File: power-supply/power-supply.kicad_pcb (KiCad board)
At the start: 2 copper layers, 100 x 100 mm, 22 parts, among them J1 Screw_Terminal_01x02, J2 Conn_01x03, J3 Conn_01x03, J4 Conn_01x03, J5 Conn_01x03, J6 Conn_01x03, J7 Conn_01x03, U1 L7815, U2 L7915

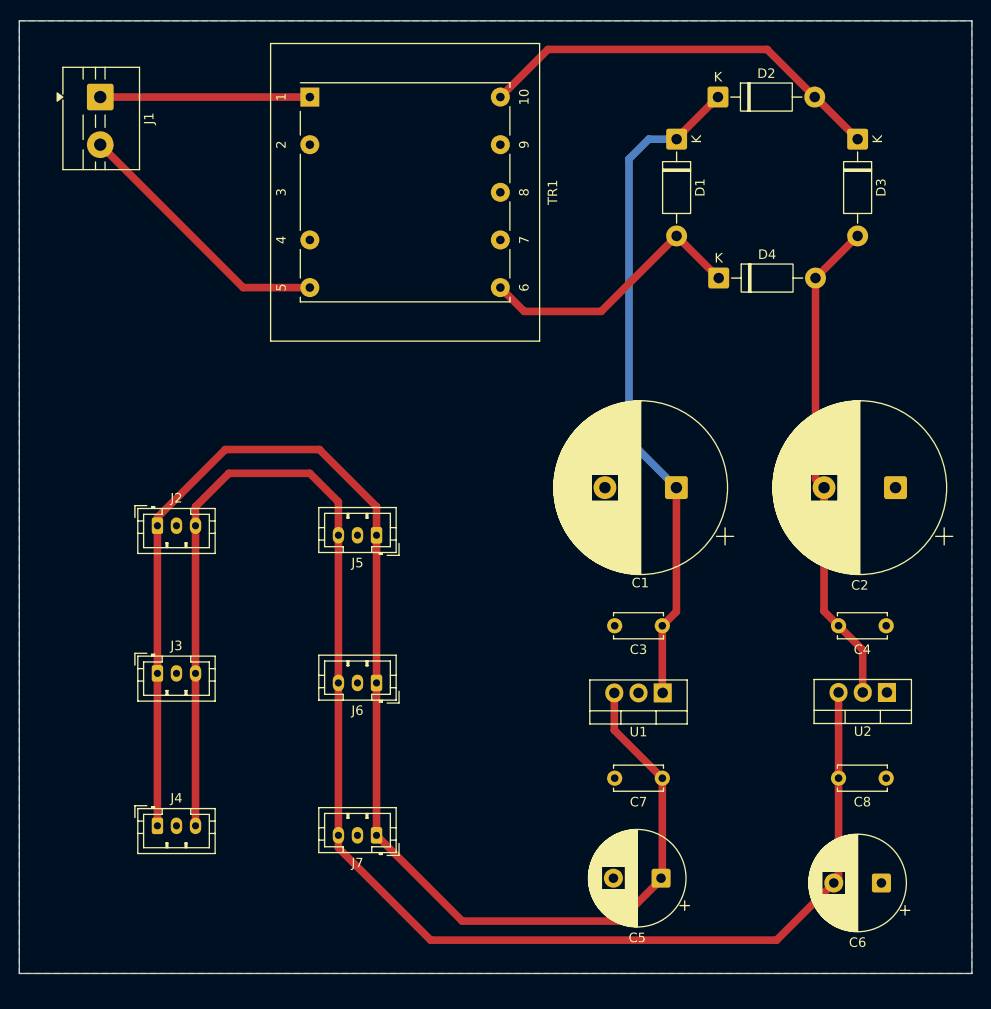
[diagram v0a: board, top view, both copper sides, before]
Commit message: power-supply: Improved version
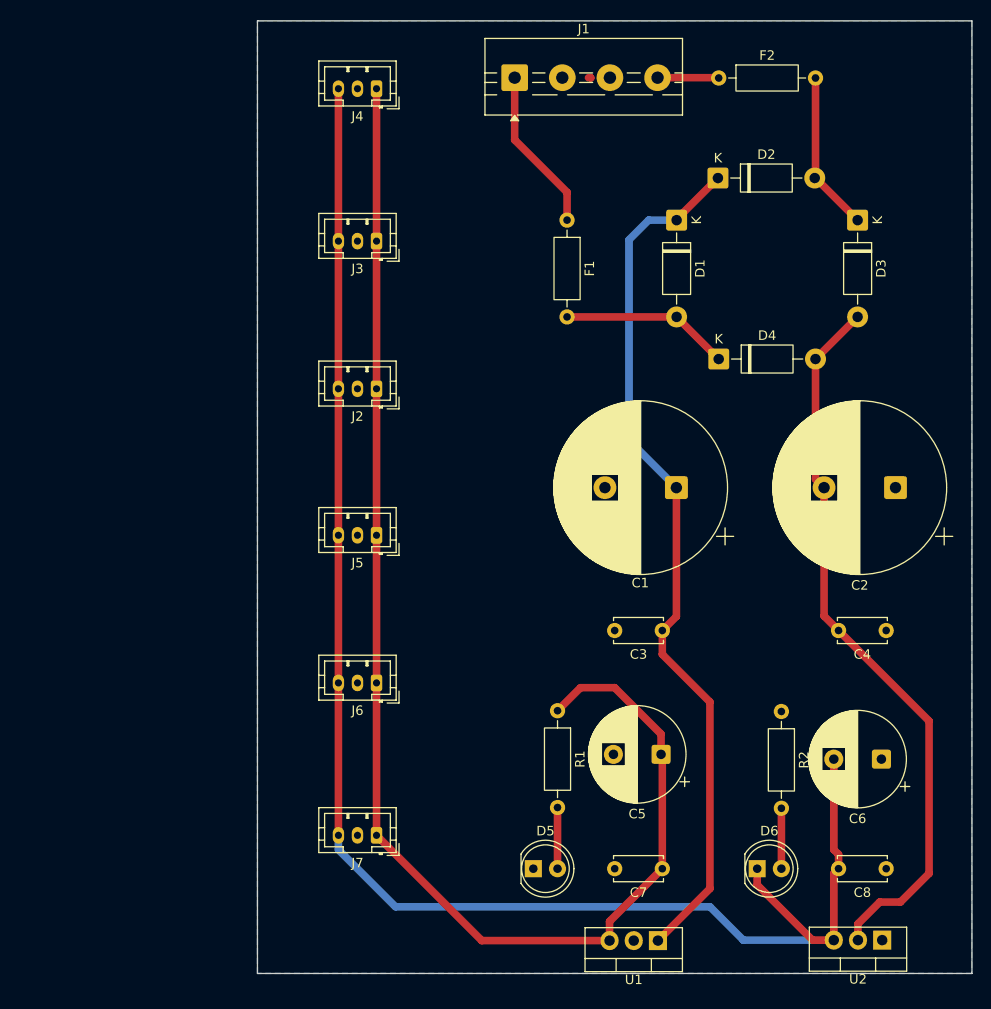
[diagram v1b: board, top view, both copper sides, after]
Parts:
- removed TR1: TEZ2.5/D230/18-18V, Transformer_THT:Transformer_Breve_TEZ-28x33
- added D5: LED, LED_THT:LED_D5.0mm, F.Cu at (204.0, 139.0)
- added D6: LED, LED_THT:LED_D5.0mm, F.Cu at (227.5, 139.0)
- added F1: Fuse, Resistor_THT:R_Axial_DIN0207_L6.3mm_D2.5mm_P10.16mm_Horizontal, F.Cu at (207.5, 70.9)
- added F2: Fuse, Resistor_THT:R_Axial_DIN0207_L6.3mm_D2.5mm_P10.16mm_Horizontal, F.Cu at (223.4, 56.0)
- added R1: R, Resistor_THT:R_Axial_DIN0207_L6.3mm_D2.5mm_P10.16mm_Horizontal, F.Cu at (206.5, 122.4)
- added R2: R, Resistor_THT:R_Axial_DIN0207_L6.3mm_D2.5mm_P10.16mm_Horizontal, F.Cu at (230.0, 122.5)
- J1: value Screw_Terminal_01x02 -> Screw_Terminal_01x04; footprint TerminalBlock:TerminalBlock_MaiXu_MX126-5.0-02P_1x02_P5.00mm -> TerminalBlock:TerminalBlock_MaiXu_MX126-5.0-04P_1x04_P5.00mm
- moved J4 80.7 mm to (187.5, 57.1), turned to 180 degrees
- moved J3 50.9 mm to (187.5, 73.1), turned to 180 degrees
- moved J1 43.5 mm to (202.0, 56.0), turned to 0 degrees
- moved J2 27.1 mm to (187.5, 88.6), turned to 180 degrees
- moved U1 26.0 mm to (217.0, 146.6)
- moved U2 26.0 mm to (240.6, 146.5)
- moved C5 13.0 mm to (217.4, 127.0)
- moved C6 13.0 mm to (240.5, 127.5)
- moved C7 9.50 mm to (217.5, 139.0)
- moved C8 9.50 mm to (241.0, 139.0)
- moved D1 8.50 mm to (219.0, 70.9)
- moved D2 8.50 mm to (223.3, 66.5)
- moved D3 8.50 mm to (238.0, 70.9)
- moved D4 8.50 mm to (223.4, 85.5)
- moved C3 0.50 mm to (217.5, 114.0)
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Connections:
- J1 pad 2: Net-(J1-Pin_2) -> GND
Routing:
- net Net-(J1-Pin_2): track 28.2 -> 0.00 mm
- net Net-(D2-A): track 43.5 -> 16.9 mm
- net Net-(D3-A): track 51.8 -> 76.6 mm
- net Net-(D1-K): track 70.8 -> 92.6 mm
- net Net-(D1-A): track 29.1 -> 17.8 mm
- net VDD: track 152.4 -> 145.3 mm
- net Net-(J1-Pin_4): track 0.00 -> 6.70 mm
- net Net-(D5-A): track 0.00 -> 6.42 mm
- net Net-(D6-A): track 0.00 -> 6.34 mm
- net Net-(J1-Pin_1): track 22.0 -> 17.2 mm
- net VEE: track 166.2 -> 167.4 mm
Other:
- board size 100 x 100 mm -> 75 x 100 mm
